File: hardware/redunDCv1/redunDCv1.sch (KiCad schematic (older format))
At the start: 16 parts, among them J1 PS1_ALARM, J10 OUT1.4, J11 OUT1.5, J12 OUT1.6, J13 OUT2.1, J14 OUT2.2, J15 OUT2.3, J16 OUT2.4, J2 PS1_PWR, J3 PS1_BAT, J4 PS2_ALARM, J5 PS2_PWR, J6 PS2_BAT, J7 OUT1.1, J8 OUT1.2, J9 OUT1.3

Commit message: first miniamal schematic is done
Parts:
- removed J10: OUT1.4, symbol Connector_Generic:Conn_01x02
- removed J11: OUT1.5, symbol Connector_Generic:Conn_01x02
- removed J8: OUT1.2, symbol Connector_Generic:Conn_01x02
- removed J9: OUT1.3, symbol Connector_Generic:Conn_01x02
- added C1, C2, C3, C4, C5, C6, C7, C8: 22µF, symbol Device:CP_Small
- added C10: 100nF, symbol Device:C_Small
- added C9: 10µF, symbol Device:CP_Small
- added D1, D10, D11, D12, D13, D14, D15, D16, D17, D18, D2, D3, D4, D5, D6, D7, D8, D9: D_Schottky, symbol Device:D_Schottky
- added D19, D21: PS1_AC-OK, symbol Device:LED
- added D20, D22: PS1_BAT-LOW, symbol Device:LED
- added F1, F2, F3, F4, F5, F6, F7, F8, F9: Polyfuse, symbol Device:Polyfuse_Small
- added J17: OUT7, symbol Connector_Generic:Conn_01x02
- added J18: OUT8, symbol Connector_Generic:Conn_01x02
- added LS1: Speaker, symbol Device:Speaker
- added Q1, Q2: BS170, Package_TO_SOT_THT:TO-92_Inline, symbol Transistor_FET:BS170
- added R1, R2, R3, R4: 1K0, symbol Device:R
- added R5, R6: 100R, symbol Device:R
- added U1: 4011, symbol 4xxx:4011
- J11: renamed from J7; value OUT1.1 -> OUT1
- J12: value OUT1.6 -> OUT2
- J13: value OUT2.1 -> OUT3
- J14: value OUT2.2 -> OUT4
- J15: value OUT2.3 -> OUT5
- J16: value OUT2.4 -> OUT6
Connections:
- net GND: now also J11.1 (Pin_1), J12.1 (Pin_1), J13.1 (Pin_1), J14.1 (Pin_1), J15.1 (Pin_1), J16.1 (Pin_1), C1.2, C10.1, C2.2, C3.2, C4.2, C5.2, C6.2, C7.2, C8.2, C9.2, J17.1 (Pin_1), J18.1 (Pin_1), Q1.3 (S), Q2.3 (S), U1.7 (VSS)
- net PS1_AC-OK: now also D19.1 (K), U1.1, U1.2
- net PS1_BAT-LOW: now also D20.1 (K), U1.6
- net PS1_V+: now also D1.2 (A), D11.2 (A), D13.2 (A), D15.2 (A), D17.2 (A), D3.2 (A), D5.2 (A), D7.2 (A), D9.2 (A)
- net PS2_AC-OK: now also D21.1 (K), U1.8, U1.9
- net PS2_BAT-LOW: now also D22.1 (K), U1.13
- net PS2_V+: now also D10.2 (A), D12.2 (A), D14.2 (A), D16.2 (A), D18.2 (A), D2.2 (A), D4.2 (A), D6.2 (A), D8.2 (A)
- net at J11.2 (Pin_2): now also C4.1, F1.1
- net at J12.2 (Pin_2): now also C1.1, F2.1
- net at J13.2 (Pin_2): now also C2.1, F3.1
- net at J14.2 (Pin_2): now also C3.1, F4.1
- net at J15.2 (Pin_2): now also C5.1, F5.1
- net at J16.2 (Pin_2): now also C6.1, F6.1
- new net: D1.1 (K), D2.1 (K), F1.2
- new net: D3.1 (K), D4.1 (K), F2.2
- new net: D5.1 (K), D6.1 (K), F3.2
- new net: D7.1 (K), D8.1 (K), F4.2
- new net: D10.1 (K), D9.1 (K), F5.2
- new net: D11.1 (K), D12.1 (K), F6.2
- new net: C7.1, F7.1, J17.2 (Pin_2)
- new net: D13.1 (K), D14.1 (K), F7.2
- new net: C8.1, F8.1, J18.2 (Pin_2)
- new net: D15.1 (K), D16.1 (K), F8.2
- new net: D17.1 (K), D18.1 (K), F9.2
- new net: D19.2 (A), R1.2
- new net: D20.2 (A), R2.2
- new net: D21.2 (A), R3.2
- new net: D22.2 (A), R4.2
- new net: U1.3, U1.5
- new net: R5.2, U1.4
- new net: U1.10, U1.12
- new net: R6.2, U1.11
- new net: LS1.2, Q1.1 (D), Q2.1 (D)
- new net: Q1.2 (G), R5.1
- new net: Q2.2 (G), R6.1
- new net +12V: C10.2, C9.1, F9.1, LS1.1, R1.1, R2.1, R3.1, R4.1, U1.14 (VDD)
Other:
- moved on the sheet: J1, J11, J2, J3, J4, J5, J6

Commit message: initial footprint assignments (WIP)
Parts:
- added H1, H2, H3, H4, H5, H6: M3, MountingHole:MountingHole_3.2mm_M3, symbol Mechanical:MountingHole
- C1, C2, C3, C4, C5, C6, C7, C8: footprint (none) -> Capacitor_Tantalum_SMD:CP_EIA-7361-438_AVX-U
- C10: footprint (none) -> Capacitor_SMD:C_0805_2012Metric
- C9: footprint (none) -> Capacitor_Tantalum_SMD:CP_EIA-6032-15_Kemet-U
- D1, D10, D11, D12, D13, D14, D15, D16, D17, D18, D2, D3, D4, D5, D6, D7, D8, D9: footprint (none) -> Diode_SMD:D_1210_3225Metric
- D19, D20, D21, D22: footprint (none) -> LED_THT:LED_D3.0mm
- F1, F2, F3, F4, F5, F6, F7, F8, F9: footprint (none) -> Fuse:Fuse_1210_3225Metric
- J1, J4: footprint (none) -> Connector_JST:JST_XH_B4B-XH-A_1x04_P2.50mm_Vertical
- J11, J12, J13, J14, J15, J16, J17, J18: footprint (none) -> TerminalBlock:TerminalBlock_Wuerth_691311400102_P7.62mm
- J2, J5: footprint (none) -> Connector_JST:JST_VH_B8P-VH_1x08_P3.96mm_Vertical
- J3, J6: footprint (none) -> TerminalBlock:TerminalBlock_Altech_AK300-2_P5.00mm
- LS1: footprint (none) -> Buzzer_Beeper:Buzzer_15x7.5RM7.6
- R1, R2, R3, R4, R5, R6: footprint (none) -> Resistor_SMD:R_0805_2012Metric
- U1: footprint (none) -> Package_SO:SOIC-14_3.9x8.7mm_P1.27mm

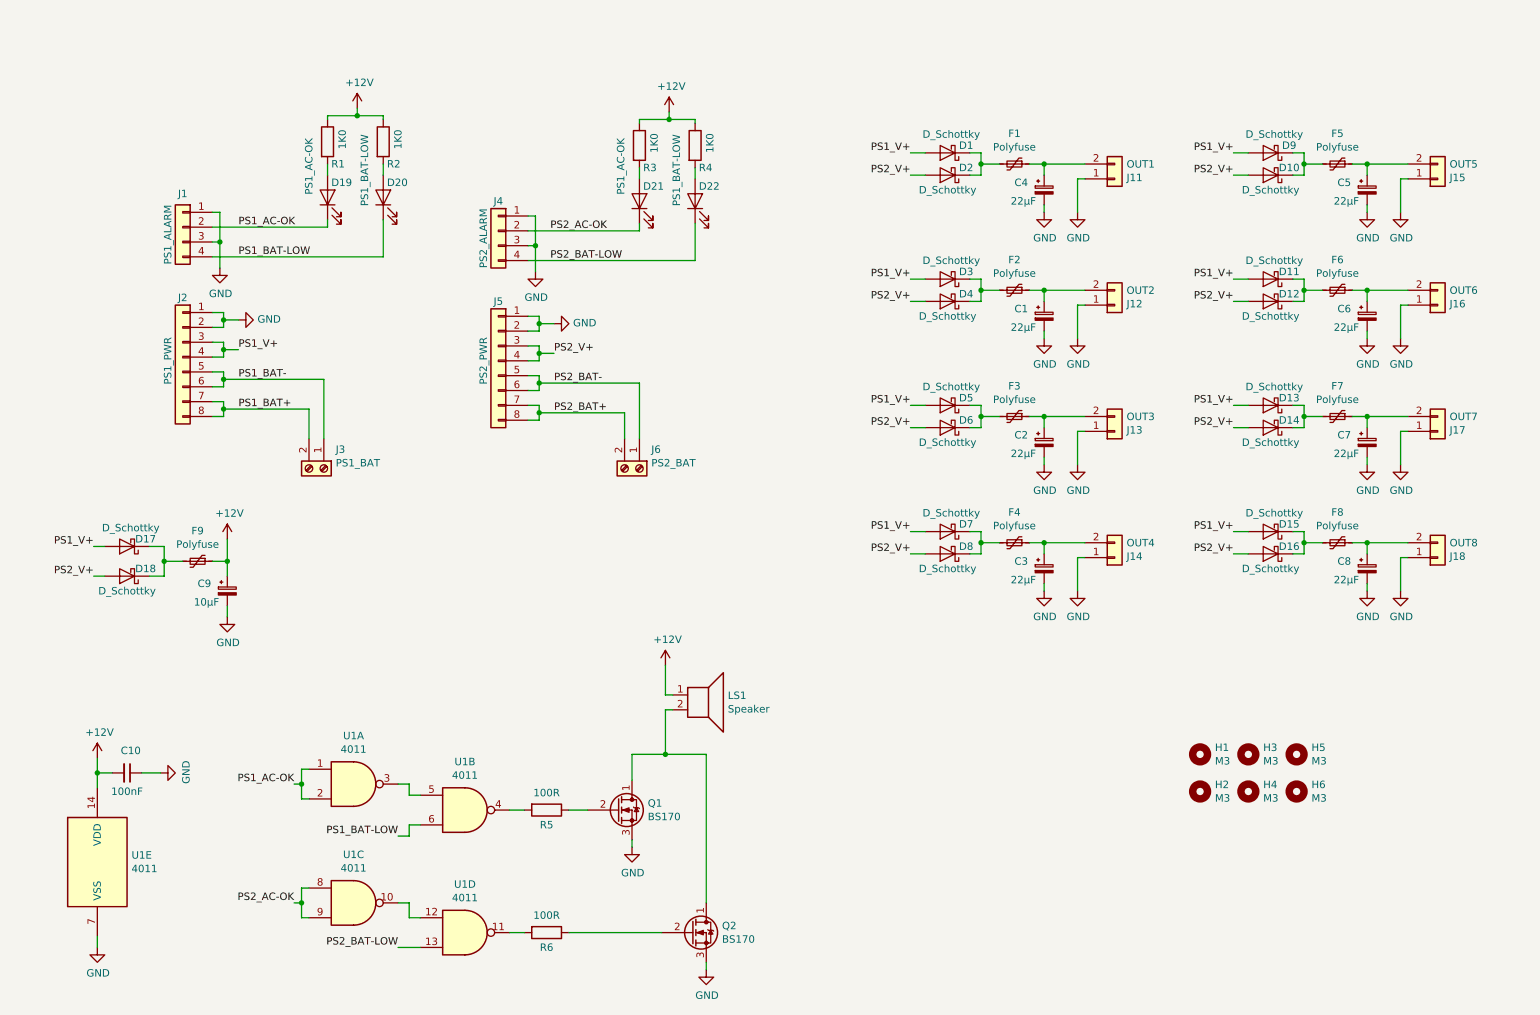
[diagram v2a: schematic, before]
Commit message: added mcu (WIP)
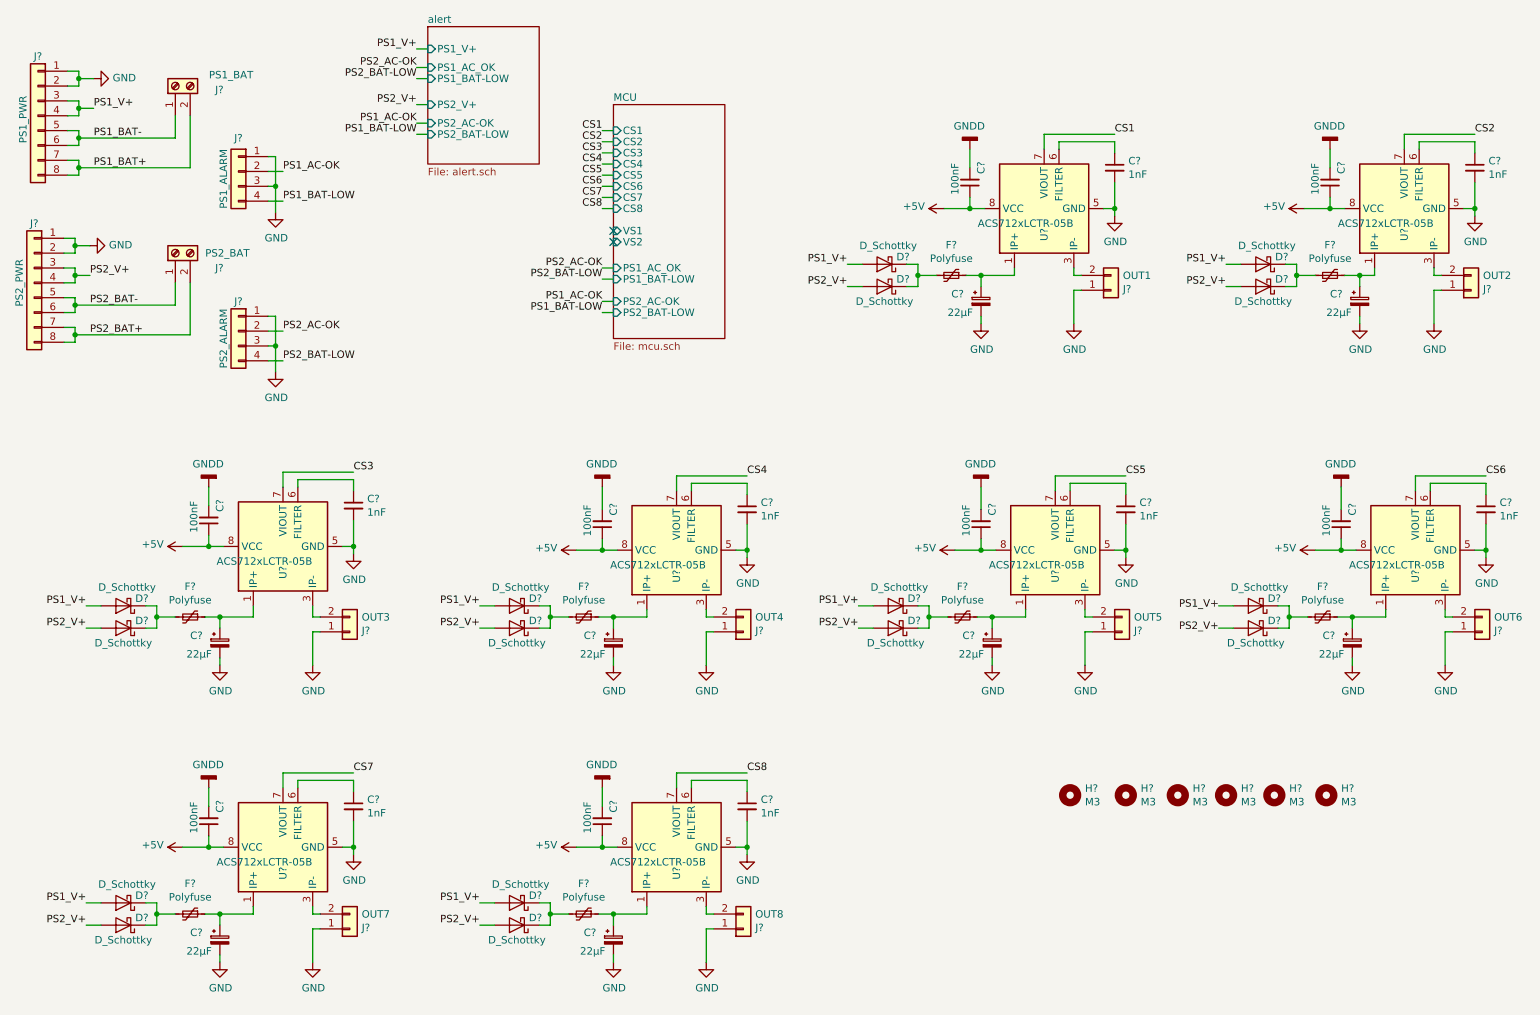
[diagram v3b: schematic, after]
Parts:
- removed C10: 100nF, Capacitor_SMD:C_0805_2012Metric, symbol Device:C_Small
- removed C9: 10µF, Capacitor_Tantalum_SMD:CP_EIA-6032-15_Kemet-U, symbol Device:CP_Small
- removed D17, D18: D_Schottky, Diode_SMD:D_1210_3225Metric, symbol Device:D_Schottky
- removed D19, D21: PS1_AC-OK, LED_THT:LED_D3.0mm, symbol Device:LED
- removed D20, D22: PS1_BAT-LOW, LED_THT:LED_D3.0mm, symbol Device:LED
- removed F9: Polyfuse, Fuse:Fuse_1210_3225Metric, symbol Device:Polyfuse_Small
- removed J1: PS1_ALARM, Connector_JST:JST_XH_B4B-XH-A_1x04_P2.50mm_Vertical, symbol Connector_Generic:Conn_01x04
- removed J4: PS2_ALARM, Connector_JST:JST_XH_B4B-XH-A_1x04_P2.50mm_Vertical, symbol Connector_Generic:Conn_01x04
- removed LS1: Speaker, Buzzer_Beeper:Buzzer_15x7.5RM7.6, symbol Device:Speaker
- removed Q1, Q2: BS170, Package_TO_SOT_THT:TO-92_Inline, symbol Transistor_FET:BS170
- removed R1, R2, R3, R4: 1K0, Resistor_SMD:R_0805_2012Metric, symbol Device:R
- removed R5, R6: 100R, Resistor_SMD:R_0805_2012Metric, symbol Device:R
- removed U1: 4011, Package_SO:SOIC-14_3.9x8.7mm_P1.27mm, symbol 4xxx:4011
- added C? (x8): 100nF, symbol Device:C_Small
- added C? (x8): 1nF, symbol Device:C_Small
- added J?: PS2_ALARM, Connector_JST:JST_XH_B4B-XH-A_1x04_P2.50mm_Vertical, symbol Connector_Generic:Conn_01x04
- added J?: PS1_ALARM, Connector_JST:JST_XH_B4B-XH-A_1x04_P2.50mm_Vertical, symbol Connector_Generic:Conn_01x04
- added U? (x8): ACS712xLCTR-05B, Package_SO:SOIC-8_3.9x4.9mm_P1.27mm, symbol Sensor_Current:ACS712xLCTR-05B
- renumbered C4 to C?, C1 to C?, C2 to C?, C3 to C?, C5 to C?, C6 to C?, C7 to C?, C8 to C?, D1 to D?, D2 to D?, D4 to D?, D3 to D?, D6 to D?, D5 to D?, D8 to D?, D7 to D?, D10 to D?, D9 to D?, D12 to D?, D11 to D?, D14 to D?, D13 to D?, D16 to D?, D15 to D?, F1 to F?, F2 to F?, F3 to F?, F4 to F?, F5 to F?, F6 to F?, F7 to F?, F8 to F?, H1 to H?, H3 to H?, H2 to H?, H4 to H?, H5 to H?, H6 to H?, J2 to J?, J5 to J?, J11 to J?, J3 to J?, J6 to J?, J12 to J?, J13 to J?, J14 to J?, J15 to J?, J16 to J?, J17 to J?, J18 to J?
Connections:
- net GND: now also C?.2, C?.2, C?.2, C?.2, C?.2, C?.2, C?.2, C?.2, J?.1 (Pin_1), J?.1 (Pin_1), J?.3 (Pin_3), J?.3 (Pin_3), U?.5 (GND), U?.5 (GND), U?.5 (GND), U?.5 (GND), U?.5 (GND), U?.5 (GND), U?.5 (GND), U?.5 (GND)
- net PS1_AC-OK: now also J?.2 (Pin_2)
- net PS1_BAT-LOW: now also J?.4 (Pin_4)
- net PS1_V+: no longer D?.2 (A)
- net PS2_AC-OK: now also J?.2 (Pin_2)
- net PS2_BAT-LOW: now also J?.4 (Pin_4)
- net PS2_V+: no longer D?.2 (A)
- net at C?.1, F?.1: now also U?.1 (IP+), U?.2 (IP+); no longer J?.2 (Pin_2) (x8)
- new net: J?.2 (Pin_2), U?.3 (IP-), U?.4 (IP-) (x8)
- new net: C?.1, U?.6 (FILTER) (x8)
- new net +5V: C?.1, C?.1, C?.1, C?.1, C?.1, C?.1, C?.1, C?.1, U?.8 (VCC), U?.8 (VCC), U?.8 (VCC), U?.8 (VCC), U?.8 (VCC), U?.8 (VCC), U?.8 (VCC), U?.8 (VCC)
- new net CS1: U?.7 (VIOUT)
- new net CS2: U?.7 (VIOUT)
- new net CS3: U?.7 (VIOUT)
- new net CS4: U?.7 (VIOUT)
- new net CS5: U?.7 (VIOUT)
- new net CS6: U?.7 (VIOUT)
- new net CS7: U?.7 (VIOUT)
- new net CS8: U?.7 (VIOUT)
- new net GNDD: C?.2, C?.2, C?.2, C?.2, C?.2, C?.2, C?.2, C?.2
- no-connect marks 0 -> 2
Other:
- moved on the sheet: C?, D?, F?, H?, J?

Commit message: schemativ almost done
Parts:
- added H? (x2): M3, MountingHole:MountingHole_3.2mm_M3, symbol Mechanical:MountingHole
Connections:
- net PS1_V+: now also D?.2 (A)
- net PS2_V+: now also D?.2 (A)
- no-connect marks 2 -> 0
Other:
- moved on the sheet: H?
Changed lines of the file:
@@
 Wire Wire Line
 	8850 4625 8950 4625
-Text Label 8850 4800 2    50   ~ 0
+Text Label 8850 4775 2    50   ~ 0
 PS2_V+
-Text Label 8850 4650 2    50   ~ 0
+Text Label 8850 4625 2    50   ~ 0
 PS1_V+
 Connection ~ 9325 4700
@@
 L Mechanical:MountingHole H?
 U 1 1 5D1B6969
-P 7850 5900
-F 0 "H?" H 7950 5946 50  0000 L CNN
-F 1 "M3" H 7950 5855 50  0000 L CNN
-F 2 "MountingHole:MountingHole_3.2mm_M3" H 7850 5900 50  0001 C CNN
-F 3 "~" H 7850 5900 50  0001 C CNN
-	1    7850 5900
+P 7800 5950
+F 0 "H?" H 7900 5996 50  0000 L CNN
+F 1 "M3" H 7900 5905 50  0000 L CNN
+F 2 "MountingHole:MountingHole_3.2mm_M3" H 7800 5950 50  0001 C CNN
+F 3 "~" H 7800 5950 50  0001 C CNN
+	1    7800 5950
 	1    0    0    -1
 $EndComp
@@
 L Mechanical:MountingHole H?
 U 1 1 5D1B6E6F
-P 8575 5900
-F 0 "H?" H 8675 5946 50  0000 L CNN
-F 1 "M3" H 8675 5855 50  0000 L CNN
-F 2 "MountingHole:MountingHole_3.2mm_M3" H 8575 5900 50  0001 C CNN
-F 3 "~" H 8575 5900 50  0001 C CNN
-	1    8575 5900
+P 8525 5950
+F 0 "H?" H 8625 5996 50  0000 L CNN
+F 1 "M3" H 8625 5905 50  0000 L CNN
+F 2 "MountingHole:MountingHole_3.2mm_M3" H 8525 5950 50  0001 C CNN
+F 3 "~" H 8525 5950 50  0001 C CNN
+	1    8525 5950
 	1    0    0    -1
 $EndComp
@@
 L Mechanical:MountingHole H?
 U 1 1 5D1B7337
-P 8225 5900
-F 0 "H?" H 8325 5946 50  0000 L CNN
-F 1 "M3" H 8325 5855 50  0000 L CNN
-F 2 "MountingHole:MountingHole_3.2mm_M3" H 8225 5900 50  0001 C CNN
-F 3 "~" H 8225 5900 50  0001 C CNN
-	1    8225 5900
+P 8175 5950
+F 0 "H?" H 8275 5996 50  0000 L CNN
+F 1 "M3" H 8275 5905 50  0000 L CNN
+F 2 "MountingHole:MountingHole_3.2mm_M3" H 8175 5950 50  0001 C CNN
+F 3 "~" H 8175 5950 50  0001 C CNN
+	1    8175 5950
 	1    0    0    -1
 $EndComp
@@
 L Mechanical:MountingHole H?
 U 1 1 5D1B76C3
-P 8900 5900
-F 0 "H?" H 9000 5946 50  0000 L CNN
-F 1 "M3" H 9000 5855 50  0000 L CNN
-F 2 "MountingHole:MountingHole_3.2mm_M3" H 8900 5900 50  0001 C CNN
-F 3 "~" H 8900 5900 50  0001 C CNN
-	1    8900 5900
+P 8850 5950
+F 0 "H?" H 8950 5996 50  0000 L CNN
+F 1 "M3" H 8950 5905 50  0000 L CNN
+F 2 "MountingHole:MountingHole_3.2mm_M3" H 8850 5950 50  0001 C CNN
+F 3 "~" H 8850 5950 50  0001 C CNN
+	1    8850 5950
 	1    0    0    -1
 $EndComp
@@
 L Mechanical:MountingHole H?
 U 1 1 5D1B7B50
-P 9225 5900
-F 0 "H?" H 9325 5946 50  0000 L CNN
-F 1 "M3" H 9325 5855 50  0000 L CNN
-F 2 "MountingHole:MountingHole_3.2mm_M3" H 9225 5900 50  0001 C CNN
-F 3 "~" H 9225 5900 50  0001 C CNN
-	1    9225 5900
+P 9175 5950
+F 0 "H?" H 9275 5996 50  0000 L CNN
+F 1 "M3" H 9275 5905 50  0000 L CNN
+F 2 "MountingHole:MountingHole_3.2mm_M3" H 9175 5950 50  0001 C CNN
+F 3 "~" H 9175 5950 50  0001 C CNN
+	1    9175 5950
 	1    0    0    -1
 $EndComp
@@
 L Mechanical:MountingHole H?
 U 1 1 5D1B7DEC
-P 9575 5900
-F 0 "H?" H 9675 5946 50  0000 L CNN
-F 1 "M3" H 9675 5855 50  0000 L CNN
-F 2 "MountingHole:MountingHole_3.2mm_M3" H 9575 5900 50  0001 C CNN
-F 3 "~" H 9575 5900 50  0001 C CNN
-	1    9575 5900
+P 9525 5950
+F 0 "H?" H 9625 5996 50  0000 L CNN
+F 1 "M3" H 9625 5905 50  0000 L CNN
+F 2 "MountingHole:MountingHole_3.2mm_M3" H 9525 5950 50  0001 C CNN
+F 3 "~" H 9525 5950 50  0001 C CNN
+	1    9525 5950
 	1    0    0    -1
 $EndComp
@@
 F10 "VS1" I L 4775 2100 50
 F11 "VS2" I L 4775 2175 50
-F12 "PS1_AC_OK" I L 4775 2350 50
 F13 "PS1_BAT-LOW" I L 4775 2425 50
 F14 "PS2_AC-OK" I L 4775 2575 50
 F15 "PS2_BAT-LOW" I L 4775 2650 50
+F16 "PS1_AC-OK" I L 4775 2350 50
 $EndSheet
 Wire Wire Line
@@
 Wire Wire Line
 	7175 1550 7175 1675
-NoConn ~ 4775 2100
-NoConn ~ 4775 2175
+Text Label 4700 2100 2    50   ~ 0
+PS1_V+
+Text Label 4700 2175 2    50   ~ 0
+PS2_V+
+Wire Wire Line
+	4700 2100 4775 2100
+Wire Wire Line
+	4775 2175 4700 2175
+$Comp
+L Mechanical:MountingHole H?
+U 1 1 5D7C5A50
+P 9875 5950
+F 0 "H?" H 9975 5996 50  0000 L CNN
+F 1 "M3" H 9975 5905 50  0000 L CNN
+F 2 "MountingHole:MountingHole_3.2mm_M3" H 9875 5950 50  0001 C CNN
+F 3 "~" H 9875 5950 50  0001 C CNN
+	1    9875 5950
+	1    0    0    -1
+$EndComp
+$Comp
+L Mechanical:MountingHole H?
+U 1 1 5D7C5A56
+P 10225 5950
+F 0 "H?" H 10325 5996 50  0000 L CNN
+F 1 "M3" H 10325 5905 50  0000 L CNN
+F 2 "MountingHole:MountingHole_3.2mm_M3" H 10225 5950 50  0001 C CNN
+F 3 "~" H 10225 5950 50  0001 C CNN
+	1    10225 5950
+	1    0    0    -1
+$EndComp
 $EndSCHEMATC
